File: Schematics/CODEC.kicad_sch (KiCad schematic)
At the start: 9 parts, among them U1 PCM3060

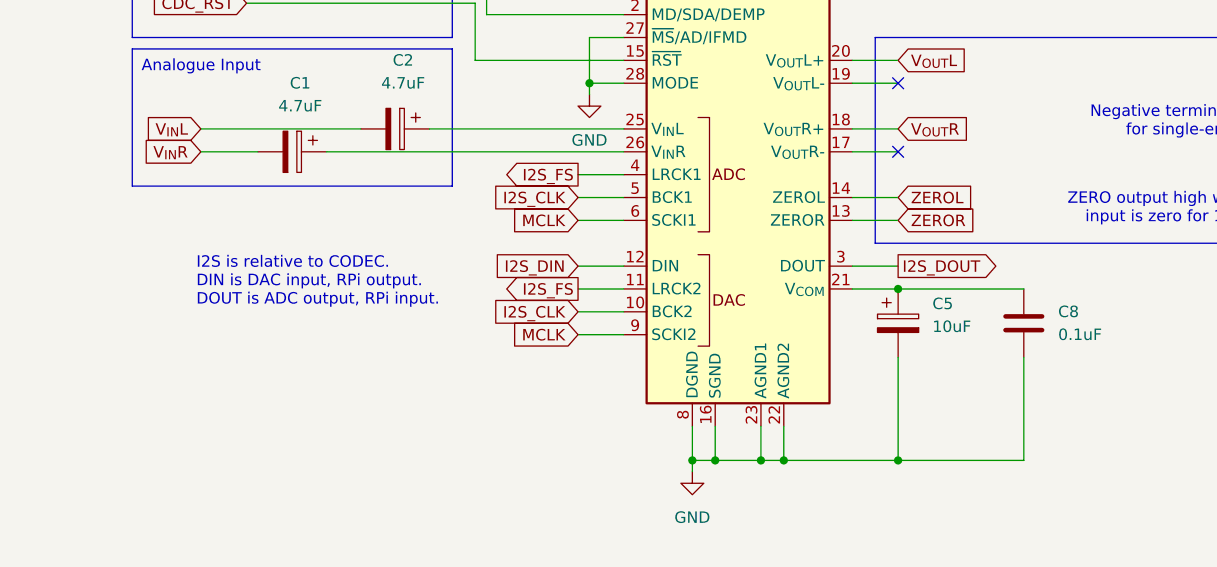
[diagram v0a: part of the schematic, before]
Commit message: Added recommended op-amps
Added recommended op-amps (without values) with dual mono TS in and out
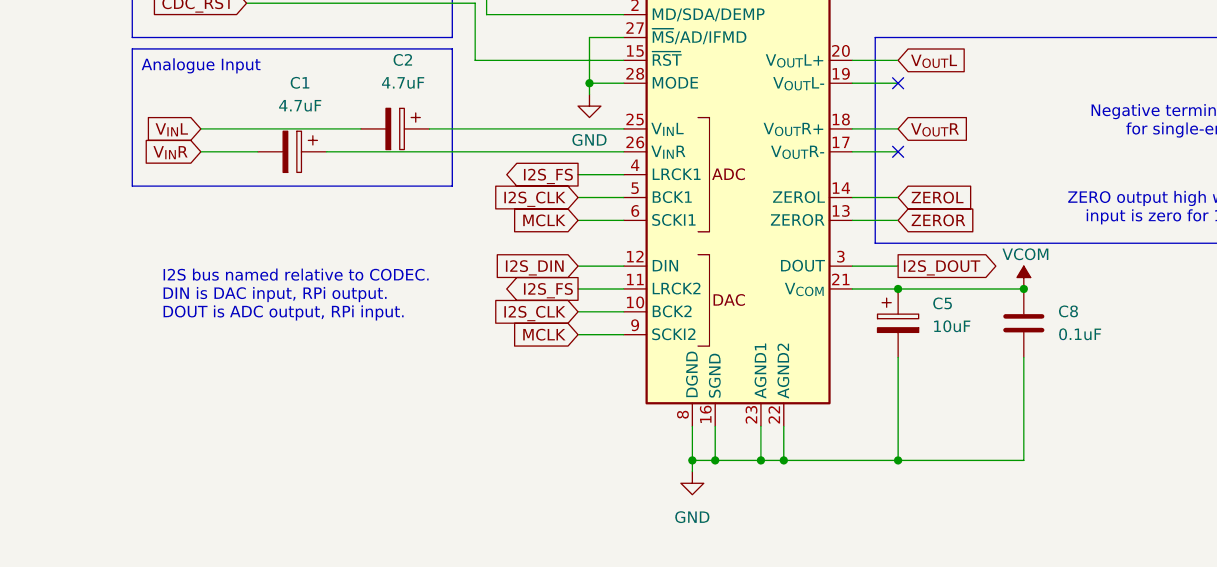
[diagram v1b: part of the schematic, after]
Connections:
- net VCOM: now reaches C5.1, C8.1, U1.21 (V_{COM})
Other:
- note added: "I2S bus named relative to CODEC. DIN is DAC input, RPi output. DOUT is ADC output, RPi input."
- note removed: "I2S is relative to CODEC. DIN is DAC input, RPi output. DOUT is ADC output, RPi input."

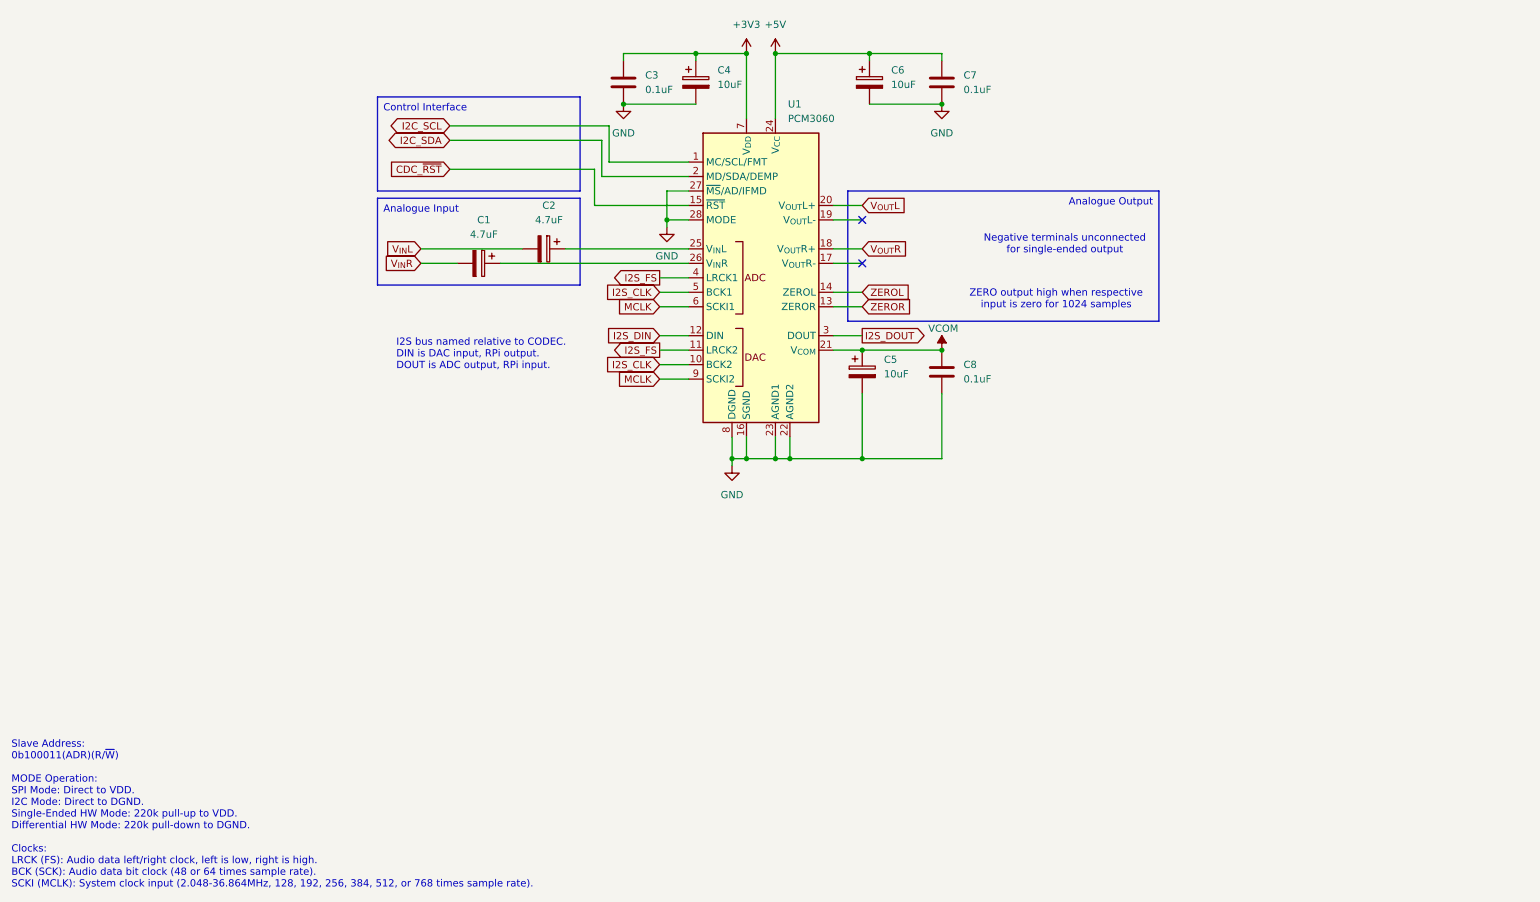
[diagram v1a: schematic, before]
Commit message: Input Buffer & EEPROM
line and instrument level buffers for the input added. EEPROM added and credits attributed !
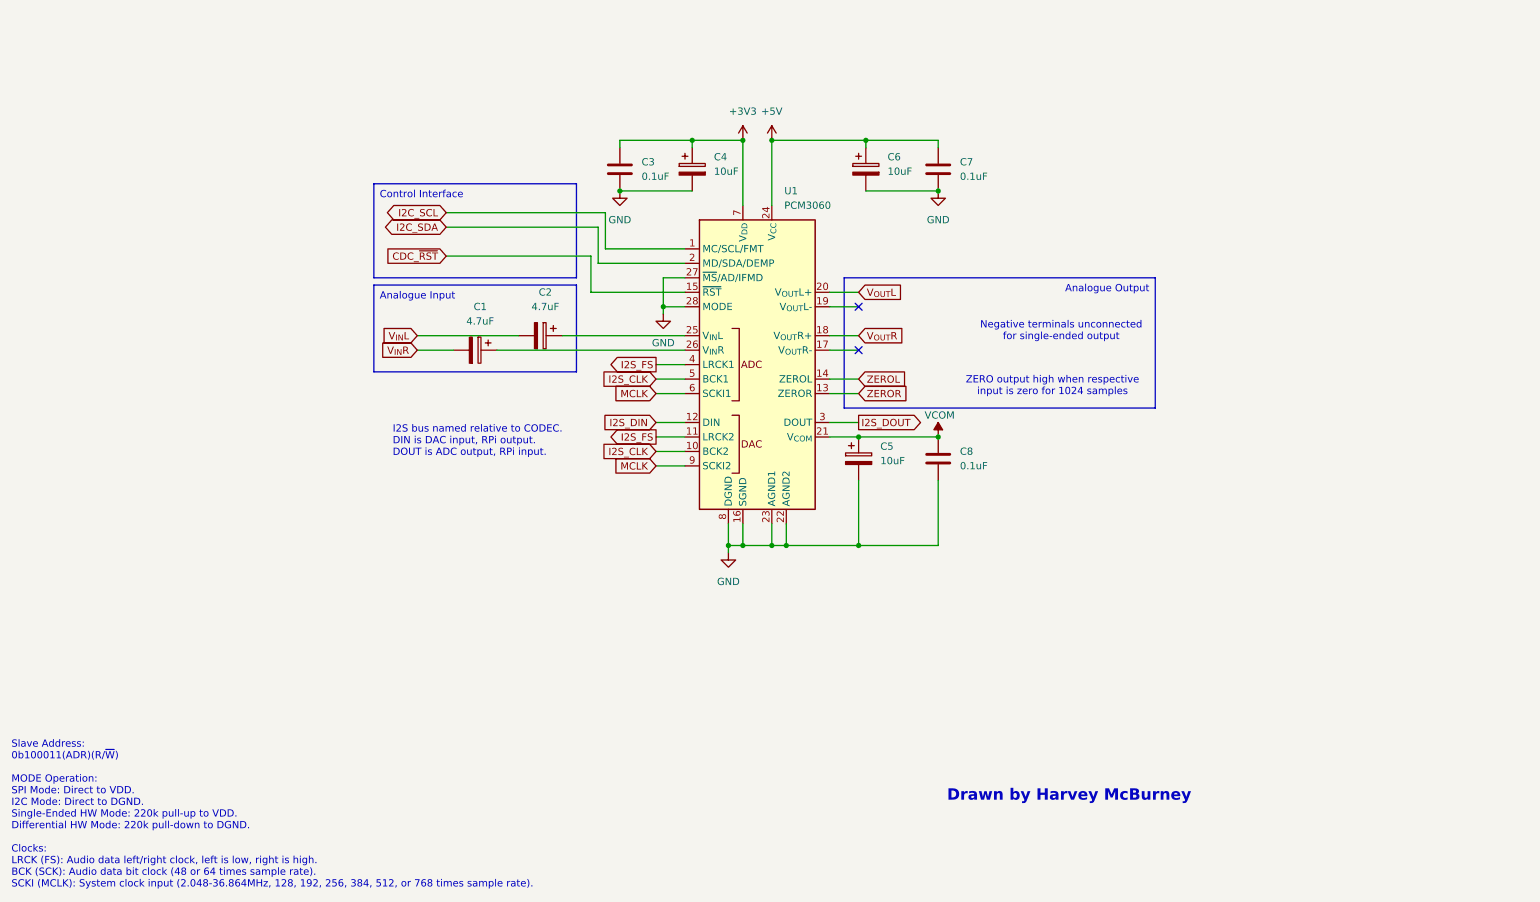
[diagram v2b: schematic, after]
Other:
- note added: "Drawn by Harvey McBurney"
- title: (none) -> CODEC SUBCIRCUIT
- moved on the sheet: C1, C2, C3, C4, C5, C6, C7, C8, U1

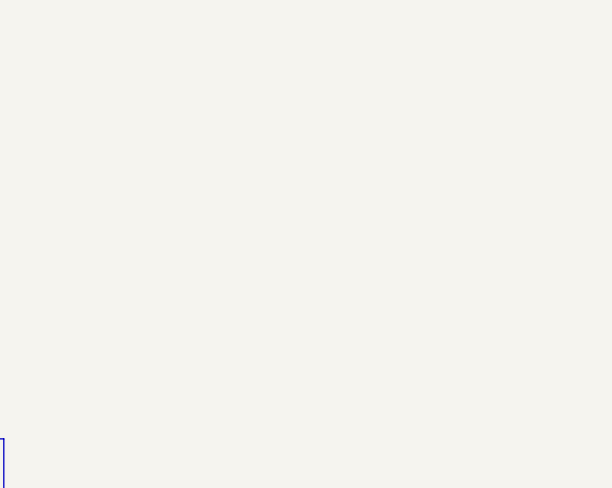
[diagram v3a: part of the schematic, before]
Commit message: Added Debug Headers
Added debug headers for I2C, I2S, and power. Also added m2.5 mounting holes for hat
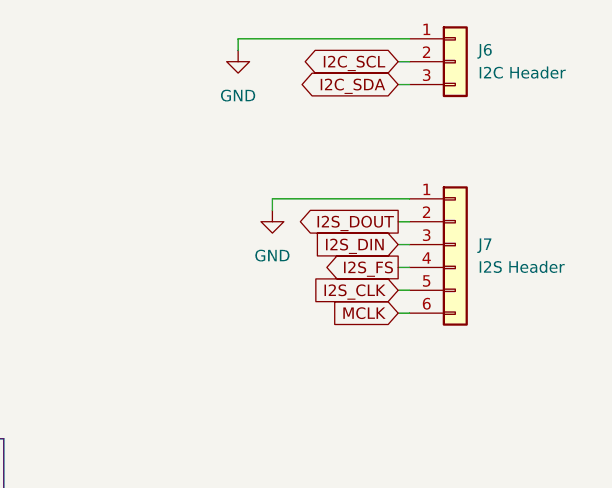
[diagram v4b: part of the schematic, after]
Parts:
- added J6: I2C Header, symbol Connector_Generic:Conn_01x03
- added J7: I2S Header, symbol Connector_Generic:Conn_01x06
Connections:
- net GND: now also J6.1 (Pin_1), J7.1 (Pin_1)
- net I2C_SCL: now also J6.2 (Pin_2)
- net I2C_SDA: now also J6.3 (Pin_3)
- net I2S_CLK: now also J7.5 (Pin_5)
- net I2S_DIN: now also J7.3 (Pin_3)
- net I2S_DOUT: now also J7.2 (Pin_2)
- net I2S_FS: now also J7.4 (Pin_4)
- net MCLK: now also J7.6 (Pin_6)

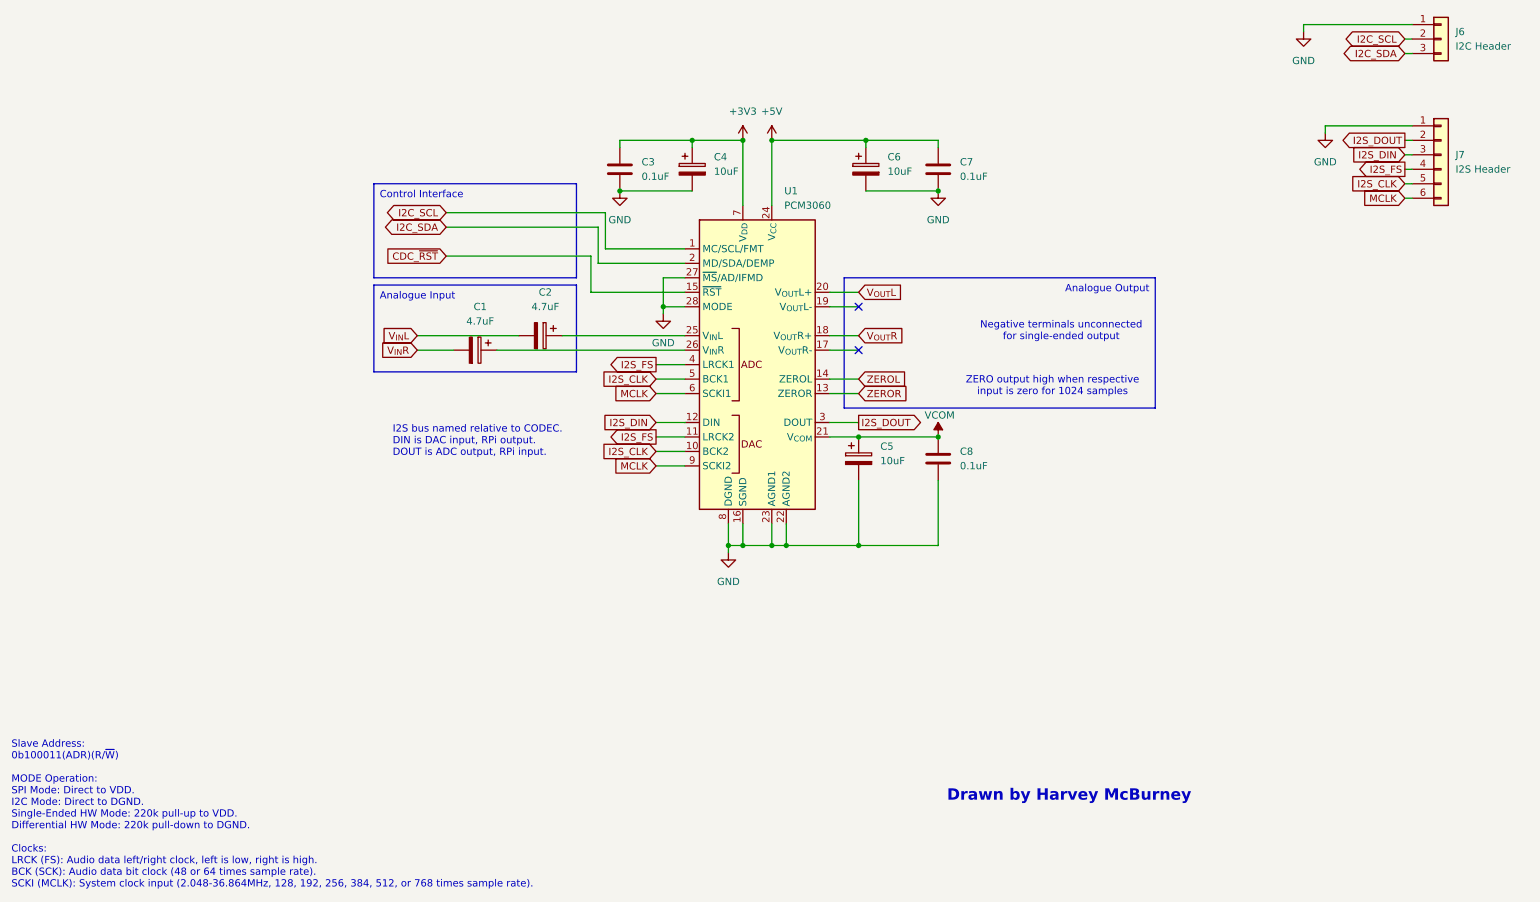
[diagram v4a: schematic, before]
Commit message: Started adding footprints, changed values.
Added footprints for most components. need to check in uni which sizes are available and what will need to be ordered from mouser.
Changed line in/out to TRS as this will be more reliable and added 0 ohm resistor options to bypass mono input and use line in/out as stereo.
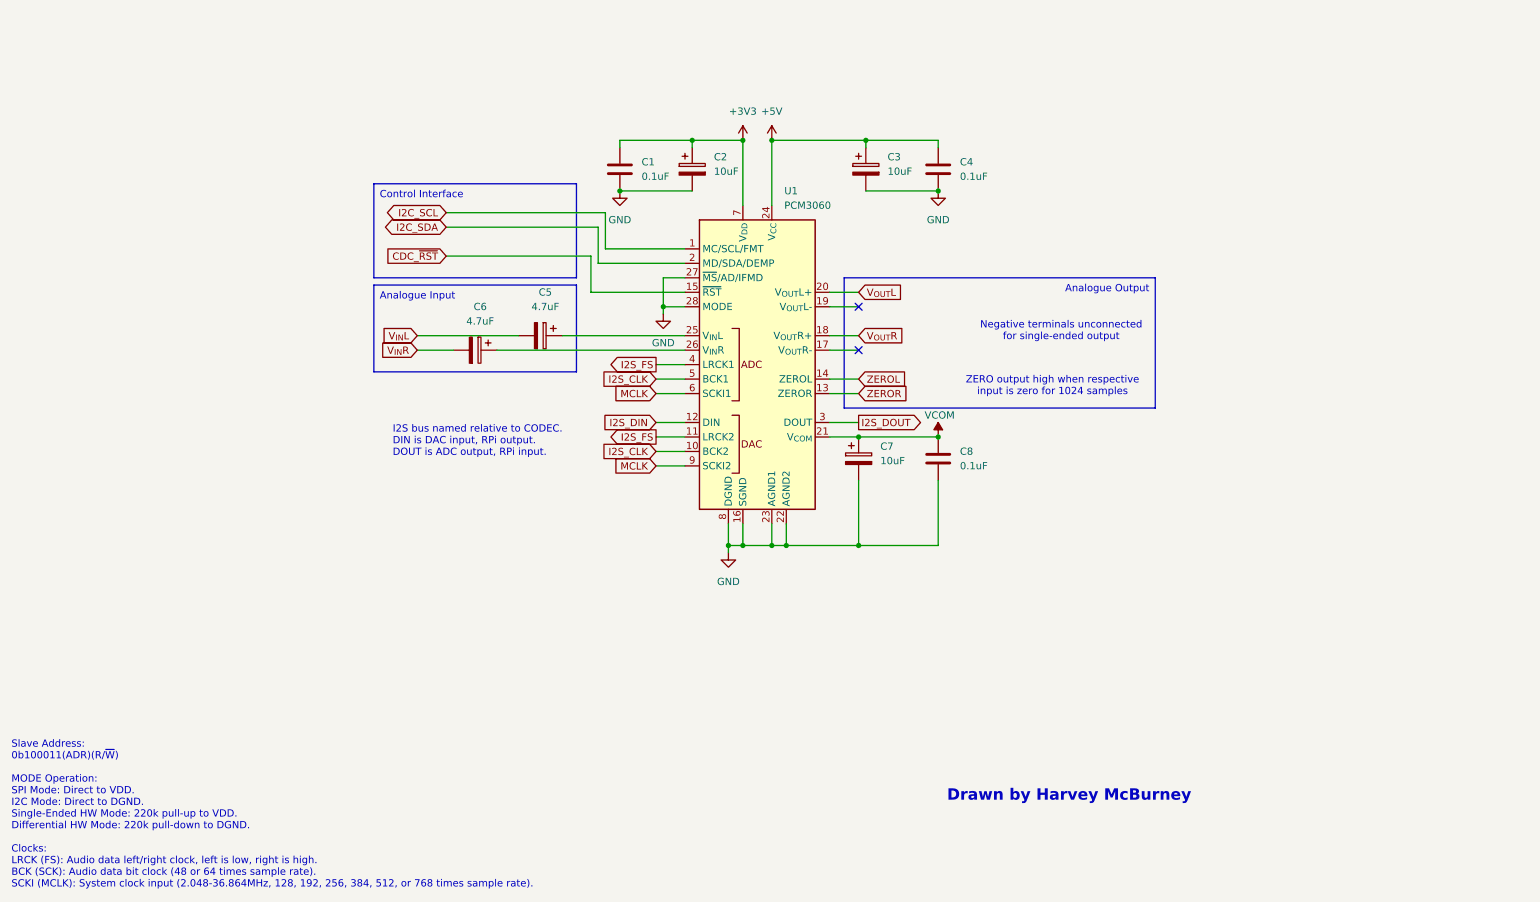
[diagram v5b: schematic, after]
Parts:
- removed J6: I2C Header, symbol Connector_Generic:Conn_01x03
- removed J7: I2S Header, symbol Connector_Generic:Conn_01x06
- renumbered C3 to C1, C4 to C2, C6 to C3, C7 to C4, C2 to C5, C1 to C6, C5 to C7
